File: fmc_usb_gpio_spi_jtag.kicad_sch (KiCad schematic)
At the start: 10 parts

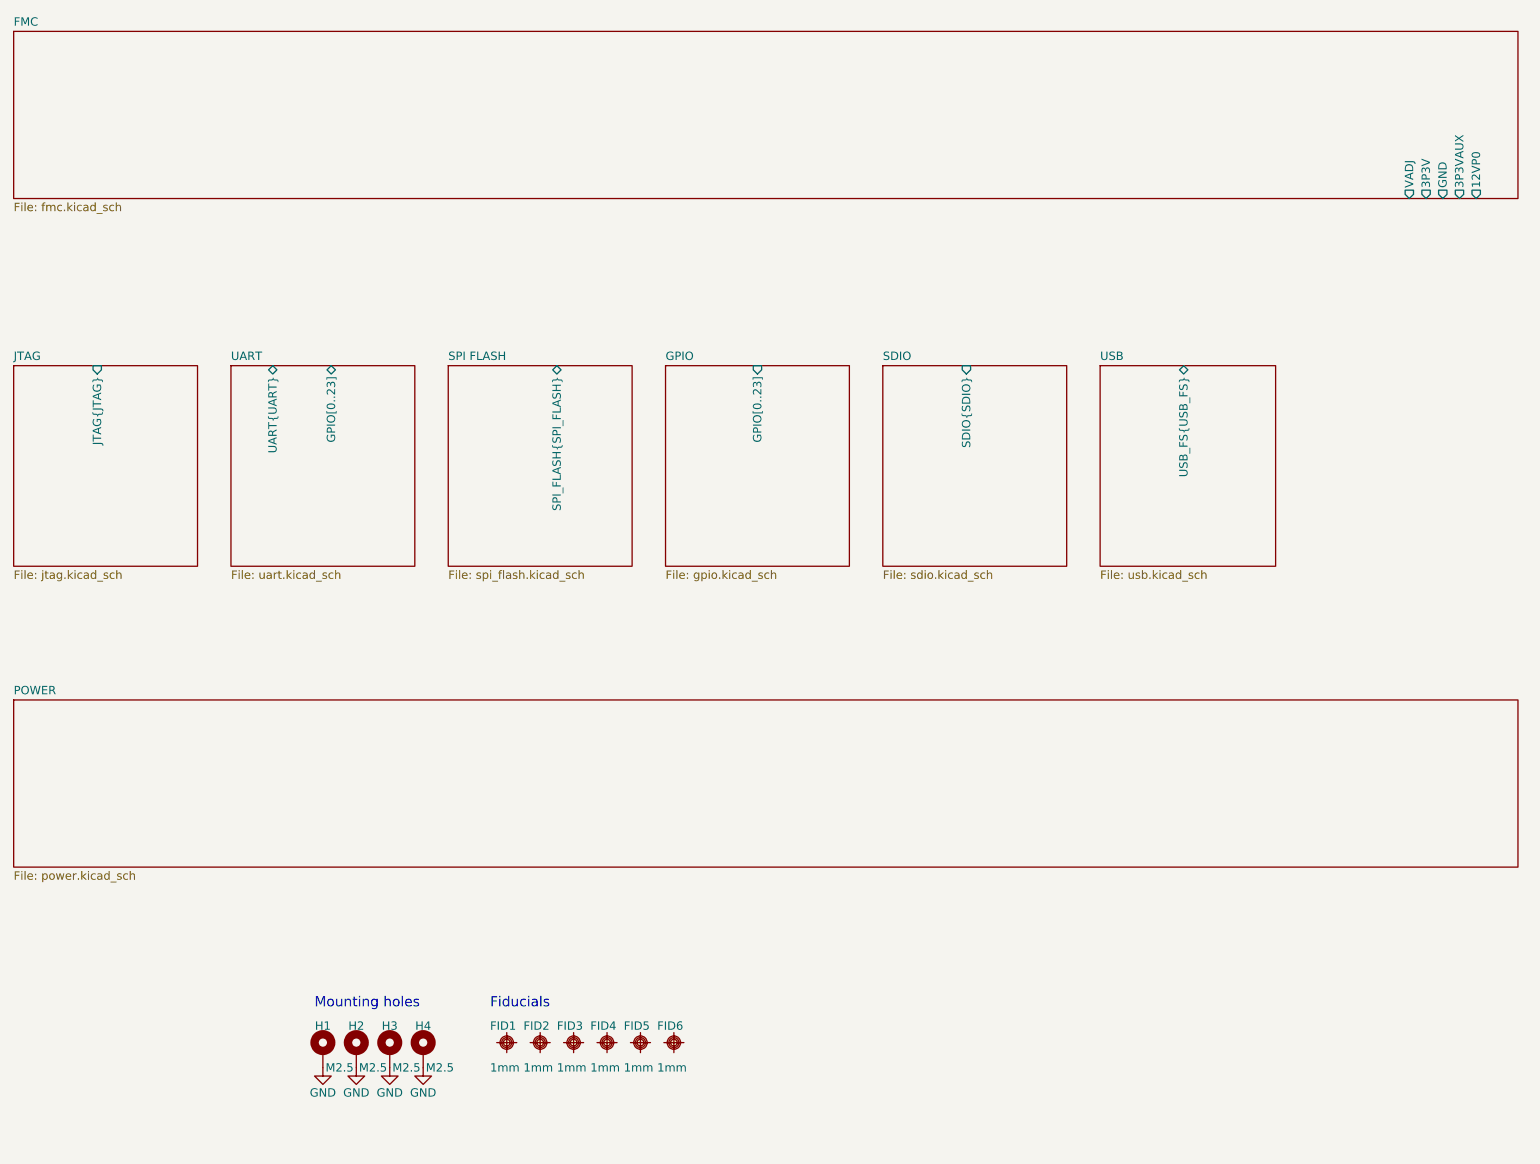
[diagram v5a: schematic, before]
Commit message: *.kicad_sch: fix sheet pin type
Signed-off-by: Huang Rui <vowstar@gmail.com>
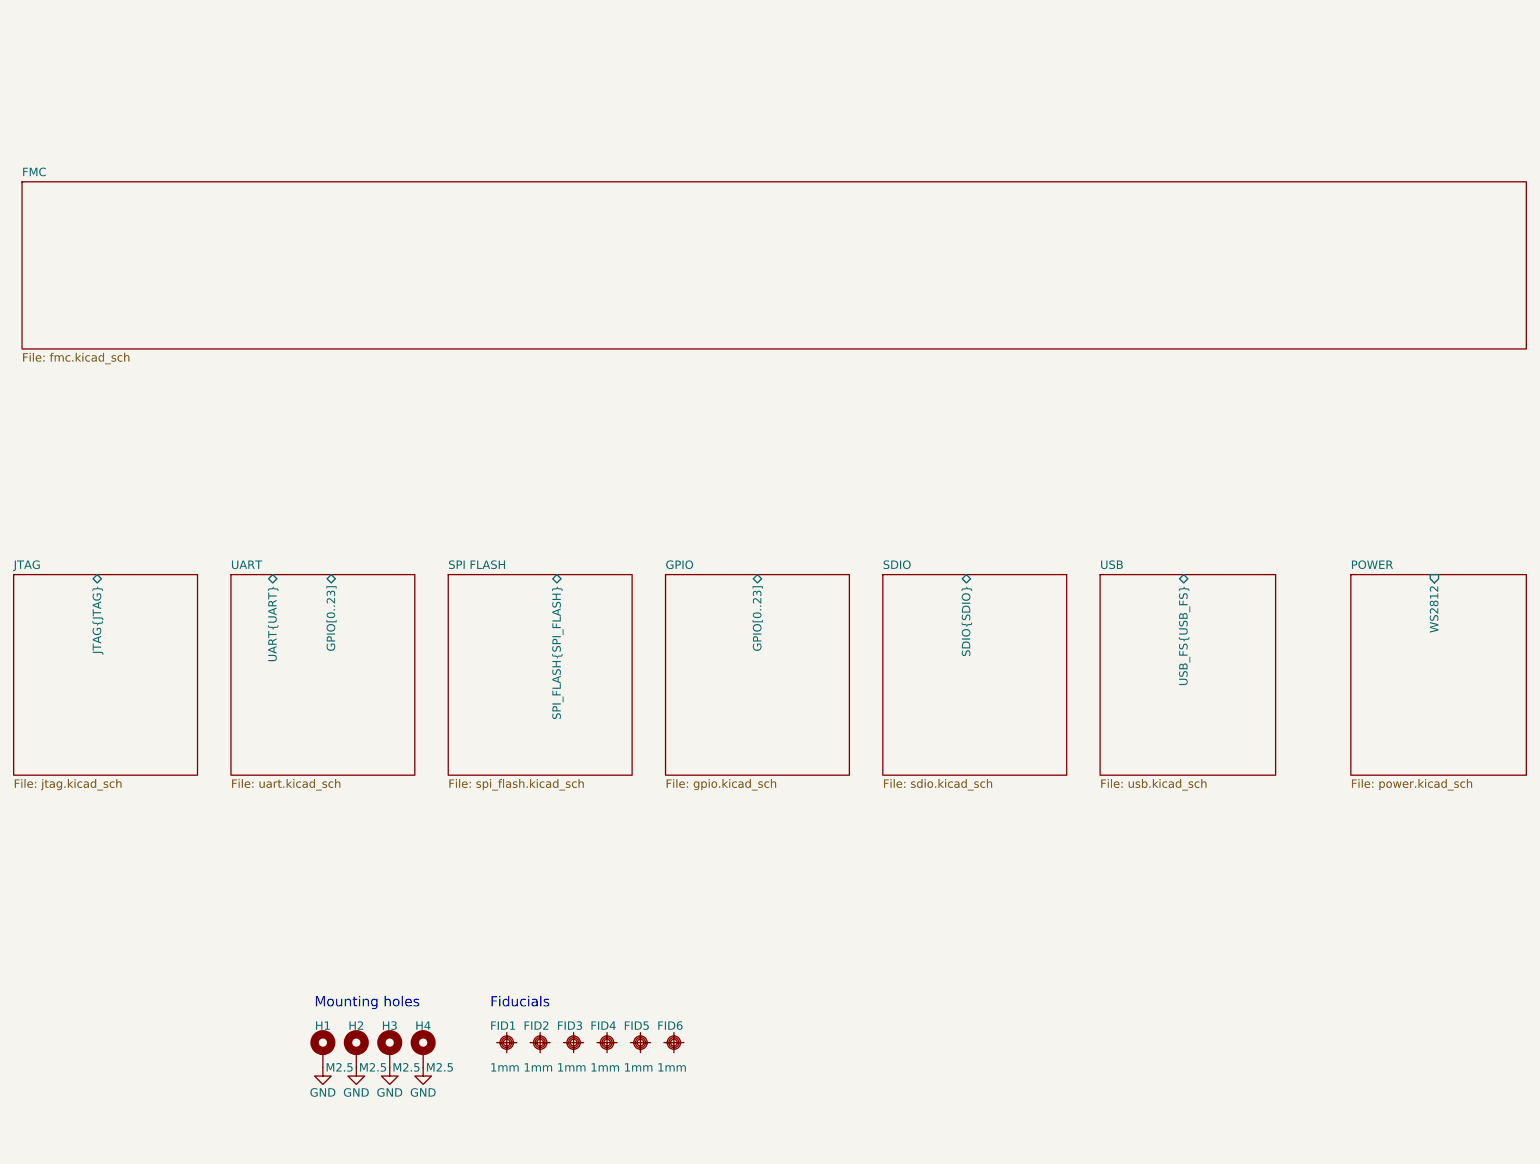
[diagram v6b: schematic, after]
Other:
- sheet FMC ports: added none; removed 12VP0, 3P3V, 3P3VAUX, GND, VADJ
- sheet POWER ports: added WS2812; removed none
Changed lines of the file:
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@@
     )
   )
-  (sheet (at 71.12 76.2) (size 27.94 30.48) (fields_autoplaced)
+  (sheet (at 71.12 107.95) (size 27.94 30.48) (fields_autoplaced)
     (stroke (width 0.1524) (type solid))
     (fill (color 0 0 0 0.0000))
-    (property "Sheetname" "UART" (at 71.12 75.4884 0)
+    (property "Sheetname" "UART" (at 71.12 107.2384 0)
       (effects (font (size 1.27 1.27)) (justify left bottom))
     )
-    (property "Sheetfile" "uart.kicad_sch" (at 71.12 107.2646 0)
+    (property "Sheetfile" "uart.kicad_sch" (at 71.12 139.0146 0)
       (effects (font (size 1.27 1.27)) (justify left top))
     )
-    (pin "UART{UART}" tri_state (at 77.47 76.2 90)
+    (pin "UART{UART}" tri_state (at 77.47 107.95 90)
       (effects (font (size 1.27 1.27)) (justify right))
     )
-    (pin "GPIO[0..23]" tri_state (at 86.36 76.2 90)
+    (pin "GPIO[0..23]" tri_state (at 86.36 107.95 90)
       (effects (font (size 1.27 1.27)) (justify right))
     )
@@
     )
   )
-  (sheet (at 38.1 25.4) (size 228.6 25.4) (fields_autoplaced)
+  (sheet (at 39.37 48.26) (size 228.6 25.4) (fields_autoplaced)
     (stroke (width 0.1524) (type solid))
     (fill (color 0 0 0 0.0000))
-    (property "Sheetname" "FMC" (at 38.1 24.6884 0)
+    (property "Sheetname" "FMC" (at 39.37 47.5484 0)
       (effects (font (size 1.27 1.27)) (justify left bottom))
     )
-    (property "Sheetfile" "fmc.kicad_sch" (at 38.1 51.3846 0)
+    (property "Sheetfile" "fmc.kicad_sch" (at 39.37 74.2446 0)
       (effects (font (size 1.27 1.27)) (justify left top))
-    )
-    (pin "12VP0" output (at 260.35 50.8 270)
-      (effects (font (size 1.27 1.27)) (justify left))
-    )
-    (pin "3P3VAUX" output (at 257.81 50.8 270)
-      (effects (font (size 1.27 1.27)) (justify left))
-    )
-    (pin "GND" output (at 255.27 50.8 270)
-      (effects (font (size 1.27 1.27)) (justify left))
-    )
-    (pin "3P3V" output (at 252.73 50.8 270)
-      (effects (font (size 1.27 1.27)) (justify left))
-    )
-    (pin "VADJ" output (at 250.19 50.8 270)
-      (effects (font (size 1.27 1.27)) (justify left))
     )
     (instances
@@
     )
   )
-  (sheet (at 203.2 76.2) (size 26.67 30.48) (fields_autoplaced)
+  (sheet (at 203.2 107.95) (size 26.67 30.48) (fields_autoplaced)
     (stroke (width 0.1524) (type solid))
     (fill (color 0 0 0 0.0000))
-    (property "Sheetname" "USB" (at 203.2 75.4884 0)
+    (property "Sheetname" "USB" (at 203.2 107.2384 0)
       (effects (font (size 1.27 1.27)) (justify left bottom))
     )
-    (property "Sheetfile" "usb.kicad_sch" (at 203.2 107.2646 0)
+    (property "Sheetfile" "usb.kicad_sch" (at 203.2 139.0146 0)
       (effects (font (size 1.27 1.27)) (justify left top))
     )
-    (pin "USB_FS{USB_FS}" bidirectional (at 215.9 76.2 90)
+    (pin "USB_FS{USB_FS}" bidirectional (at 215.9 107.95 90)
       (effects (font (size 1.27 1.27)) (justify right))
     )
@@
     )
   )
-  (sheet (at 38.1 76.2) (size 27.94 30.48) (fields_autoplaced)
+  (sheet (at 38.1 107.95) (size 27.94 30.48) (fields_autoplaced)
     (stroke (width 0.1524) (type solid))
     (fill (color 0 0 0 0.0000))
-    (property "Sheetname" "JTAG" (at 38.1 75.4884 0)
+    (property "Sheetname" "JTAG" (at 38.1 107.2384 0)
       (effects (font (size 1.27 1.27)) (justify left bottom))
     )
-    (property "Sheetfile" "jtag.kicad_sch" (at 38.1 107.2646 0)
+    (property "Sheetfile" "jtag.kicad_sch" (at 38.1 139.0146 0)
       (effects (font (size 1.27 1.27)) (justify left top))
     )
-    (pin "JTAG{JTAG}" input (at 50.8 76.2 90)
+    (pin "JTAG{JTAG}" bidirectional (at 50.8 107.95 90)
       (effects (font (size 1.27 1.27)) (justify right))
     )
@@
     )
   )
-  (sheet (at 137.16 76.2) (size 27.94 30.48) (fields_autoplaced)
+  (sheet (at 137.16 107.95) (size 27.94 30.48) (fields_autoplaced)
     (stroke (width 0.1524) (type solid))
     (fill (color 0 0 0 0.0000))
-    (property "Sheetname" "GPIO" (at 137.16 75.4884 0)
+    (property "Sheetname" "GPIO" (at 137.16 107.2384 0)
       (effects (font (size 1.27 1.27)) (justify left bottom))
     )
-    (property "Sheetfile" "gpio.kicad_sch" (at 137.16 107.2646 0)
+    (property "Sheetfile" "gpio.kicad_sch" (at 137.16 139.0146 0)
       (effects (font (size 1.27 1.27)) (justify left top))
     )
-    (pin "GPIO[0..23]" input (at 151.13 76.2 90)
+    (pin "GPIO[0..23]" bidirectional (at 151.13 107.95 90)
       (effects (font (size 1.27 1.27)) (justify right))
     )
@@
     )
   )
-  (sheet (at 38.1 127) (size 228.6 25.4) (fields_autoplaced)
+  (sheet (at 241.3 107.95) (size 26.67 30.48) (fields_autoplaced)
     (stroke (width 0.1524) (type solid))
     (fill (color 0 0 0 0.0000))
-    (property "Sheetname" "POWER" (at 38.1 126.2884 0)
+    (property "Sheetname" "POWER" (at 241.3 107.2384 0)
       (effects (font (size 1.27 1.27)) (justify left bottom))
     )
-    (property "Sheetfile" "power.kicad_sch" (at 38.1 152.9846 0)
+    (property "Sheetfile" "power.kicad_sch" (at 241.3 139.0146 0)
       (effects (font (size 1.27 1.27)) (justify left top))
+    )
+    (pin "WS2812" input (at 254 107.95 90)
+      (effects (font (size 1.27 1.27)) (justify right))
     )
     (instances
@@
     )
   )
-  (sheet (at 104.14 76.2) (size 27.94 30.48) (fields_autoplaced)
+  (sheet (at 104.14 107.95) (size 27.94 30.48) (fields_autoplaced)
     (stroke (width 0.1524) (type solid))
     (fill (color 0 0 0 0.0000))
-    (property "Sheetname" "SPI FLASH" (at 104.14 75.4884 0)
+    (property "Sheetname" "SPI FLASH" (at 104.14 107.2384 0)
       (effects (font (size 1.27 1.27)) (justify left bottom))
     )
-    (property "Sheetfile" "spi_flash.kicad_sch" (at 104.14 107.2646 0)
+    (property "Sheetfile" "spi_flash.kicad_sch" (at 104.14 139.0146 0)
       (effects (font (size 1.27 1.27)) (justify left top))
     )
-    (pin "SPI_FLASH{SPI_FLASH}" bidirectional (at 120.65 76.2 90)
+    (pin "SPI_FLASH{SPI_FLASH}" bidirectional (at 120.65 107.95 90)
       (effects (font (size 1.27 1.27)) (justify right))
     )
@@
     )
   )
-  (sheet (at 170.18 76.2) (size 27.94 30.48) (fields_autoplaced)
+  (sheet (at 170.18 107.95) (size 27.94 30.48) (fields_autoplaced)
     (stroke (width 0.1524) (type solid))
     (fill (color 0 0 0 0.0000))
-    (property "Sheetname" "SDIO" (at 170.18 75.4884 0)
+    (property "Sheetname" "SDIO" (at 170.18 107.2384 0)
       (effects (font (size 1.27 1.27)) (justify left bottom))
     )
-    (property "Sheetfile" "sdio.kicad_sch" (at 170.18 107.2646 0)
+    (property "Sheetfile" "sdio.kicad_sch" (at 170.18 139.0146 0)
       (effects (font (size 1.27 1.27)) (justify left top))
     )
-    (pin "SDIO{SDIO}" input (at 182.88 76.2 90)
+    (pin "SDIO{SDIO}" bidirectional (at 182.88 107.95 90)
       (effects (font (size 1.27 1.27)) (justify right))
     )

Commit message: *.kicad_sch: apply new template styles
Signed-off-by: Huang Rui <vowstar@gmail.com>
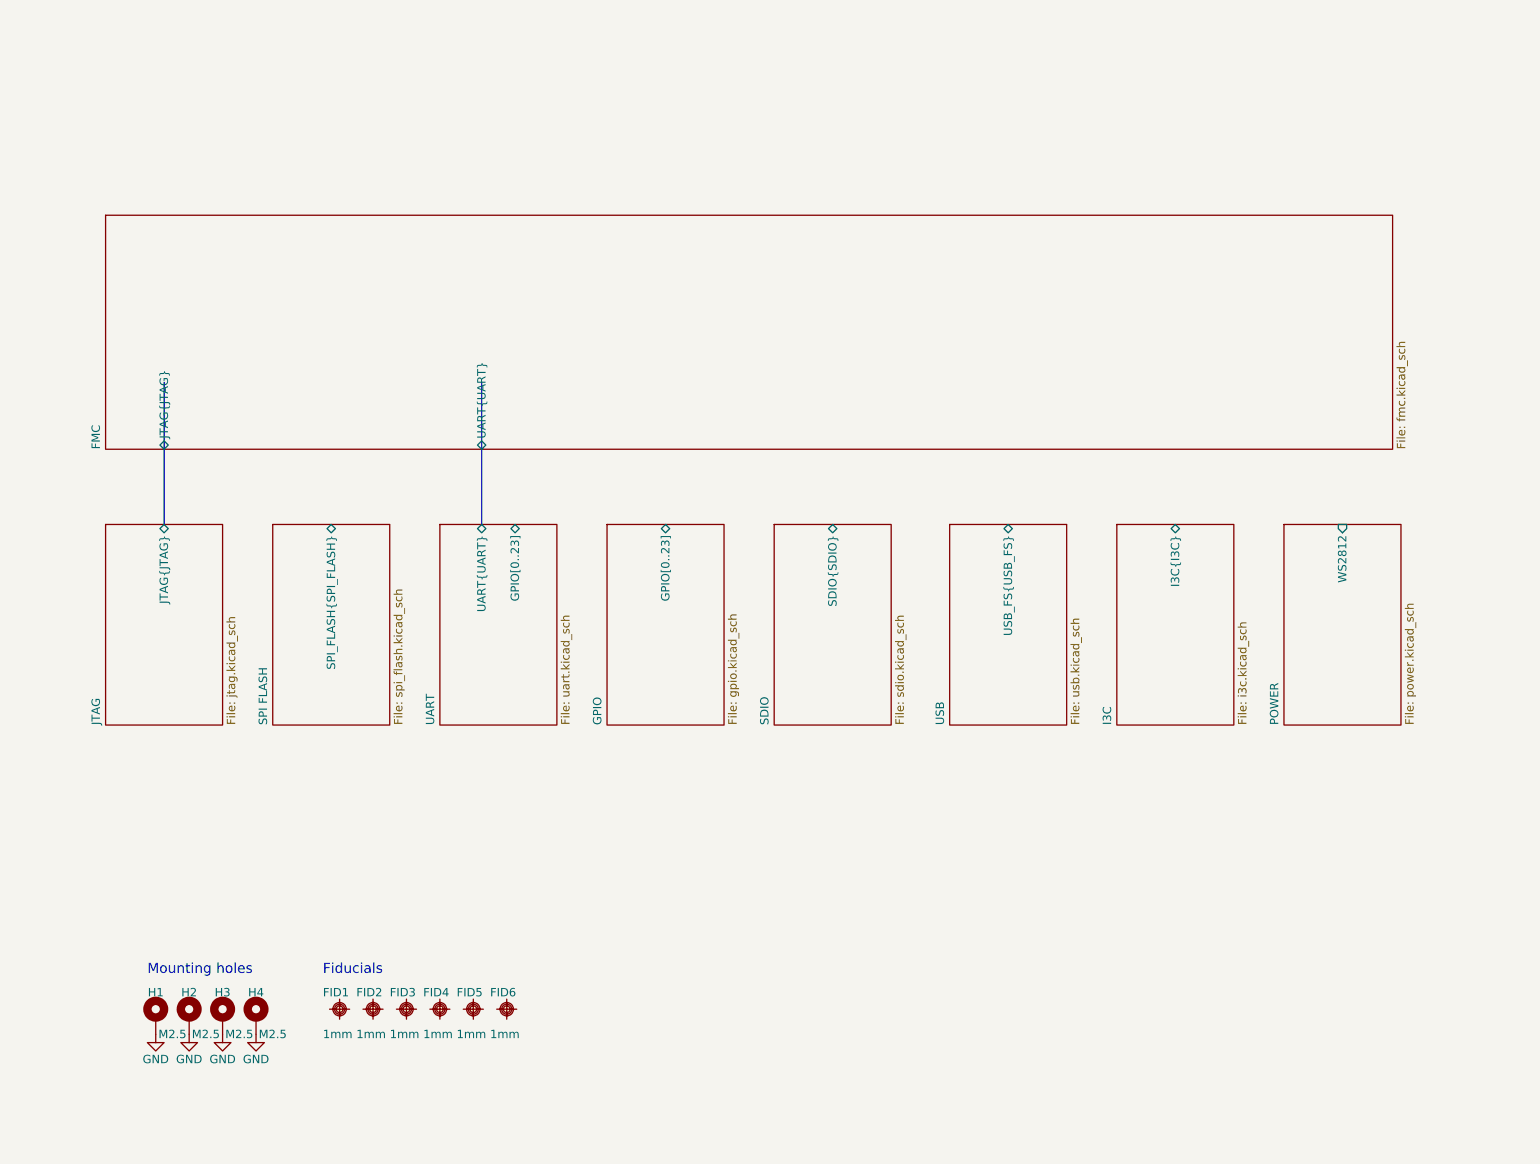
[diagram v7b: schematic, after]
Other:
- added sheet I3C (i3c.kicad_sch)
- sheet FMC ports: added JTAG{JTAG}, UART{UART}; removed none
- company: (none) -> CHIPS Alliance
- title: (none) -> FMC of Basic Peripherals for rocket chips
- moved on the sheet: FID1, FID2, FID3, FID4, FID5, FID6, H1, H2, H3, H4
